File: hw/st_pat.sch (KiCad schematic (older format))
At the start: 18 parts, among them J1 Feather Left, J2 Feather Right, J3 SHARP Display, J4 BATTERY, J5 Compass Left, J6 Compass Right, SW1 SW_PWR, SW2 BTN_RST, SW3 BTN, SW4 BTN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

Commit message: Found symbol and footprint for adafruit feather
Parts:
- removed J1: Feather Left, symbol Connector:Conn_01x16_Female
- removed J2: Feather Right, symbol Connector:Conn_01x12_Female
- removed SW1: SW_PWR, symbol Switch:SW_SPST
- added SW1: SW_PWR, st_pats:SW_Rocker_A22K1H-EA, symbol Switch:SW_Push_DPDT
- added U2: FEATHER_M0_BASIC_PROTO, st_pats:MODULE_FEATHER_M0_BASIC_PROTO, symbol FEATHER_M0_BASIC_PROTO:FEATHER_M0_BASIC_PROTO
- C1, C2: footprint (none) -> Capacitor_SMD:C_0805_2012Metric_Pad1.18x1.45mm_HandSolder
- D1, D2: footprint (none) -> LED_SMD:LED_1206_3216Metric_Pad1.42x1.75mm_HandSolder
- J3: footprint (none) -> Connector_PinHeader_2.54mm:PinHeader_1x09_P2.54mm_Vertical
- J4: footprint (none) -> Connector:JWT_A3963_1x02_P3.96mm_Vertical
- J5: value Compass Left -> Compass Right; footprint (none) -> Connector_PinHeader_2.54mm:PinHeader_1x04_P2.54mm_Vertical
- J6: value Compass Right -> Compass Left; footprint (none) -> Connector_PinHeader_2.54mm:PinHeader_1x06_P2.54mm_Vertical
- R1, R2: footprint (none) -> Resistor_SMD:R_0805_2012Metric_Pad1.20x1.40mm_HandSolder
- SW2, SW3, SW4, SW5: footprint (none) -> st_pats:SW_Mini_Soft
- U1: footprint (none) -> st_pats:FGPMMOPA6H
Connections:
- net labels removed: 3v3, A0, AREF, D13, D9, EN, SCI, SDA, VBAT, VBUS
- wire segments 36 -> 35
- no-connect marks 16 -> 20
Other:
- note added: "FEATHER M0 ADALOGGER"
- note removed: "FEATHER M0 ADALOGGER PINS"
- moved on the sheet: D2, J4, J5, J6, R2

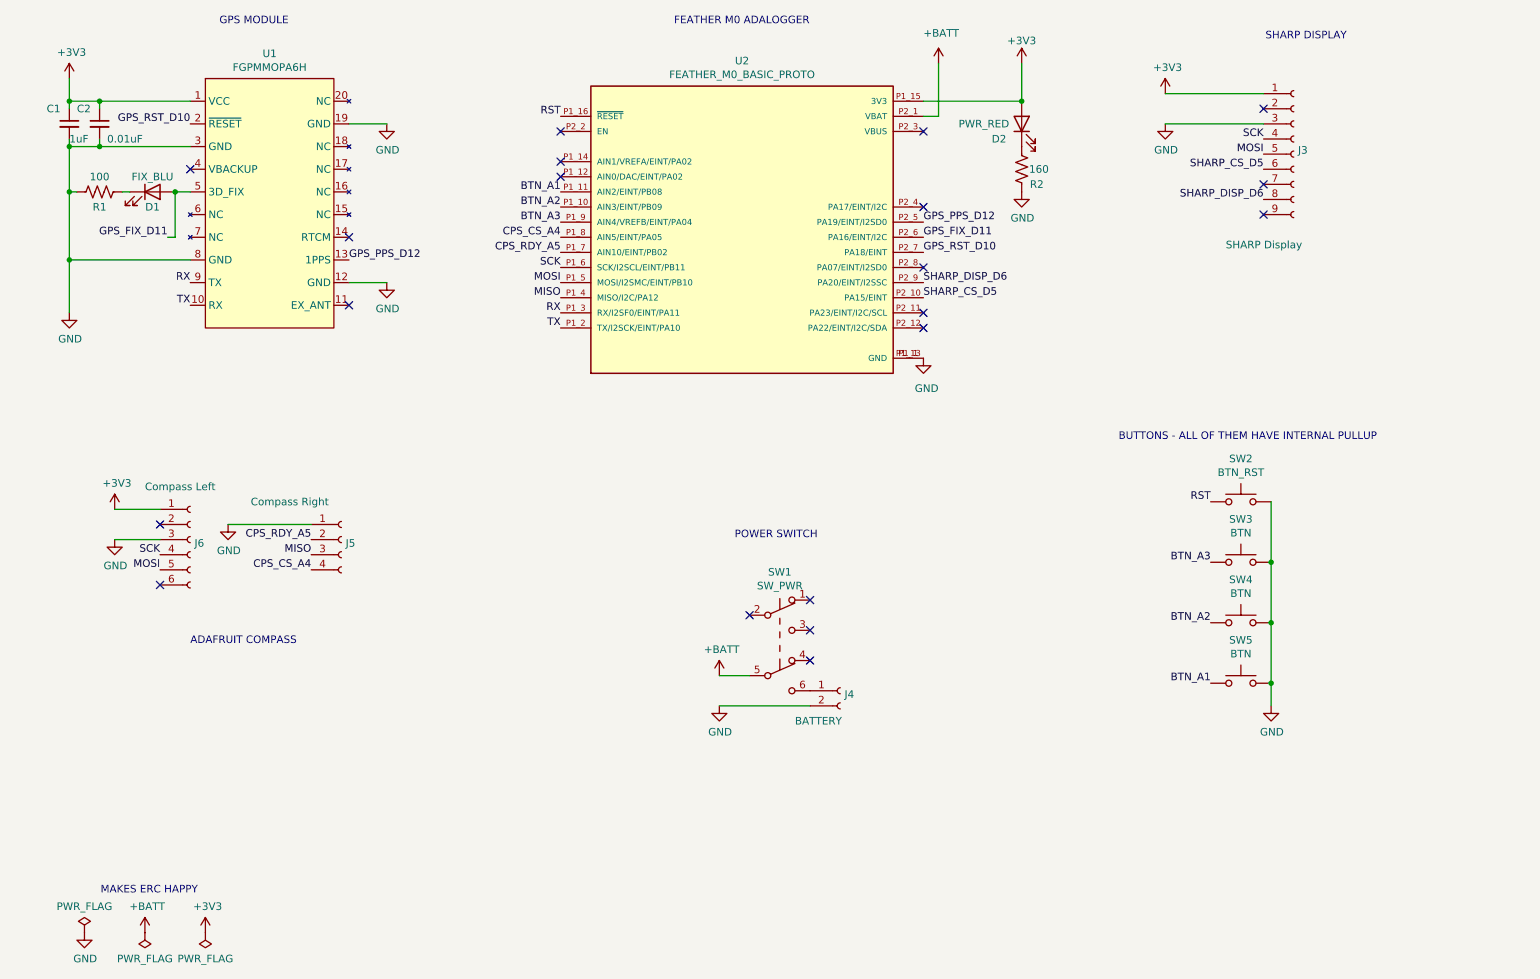
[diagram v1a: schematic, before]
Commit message: Add one more led to schematic and create pcb
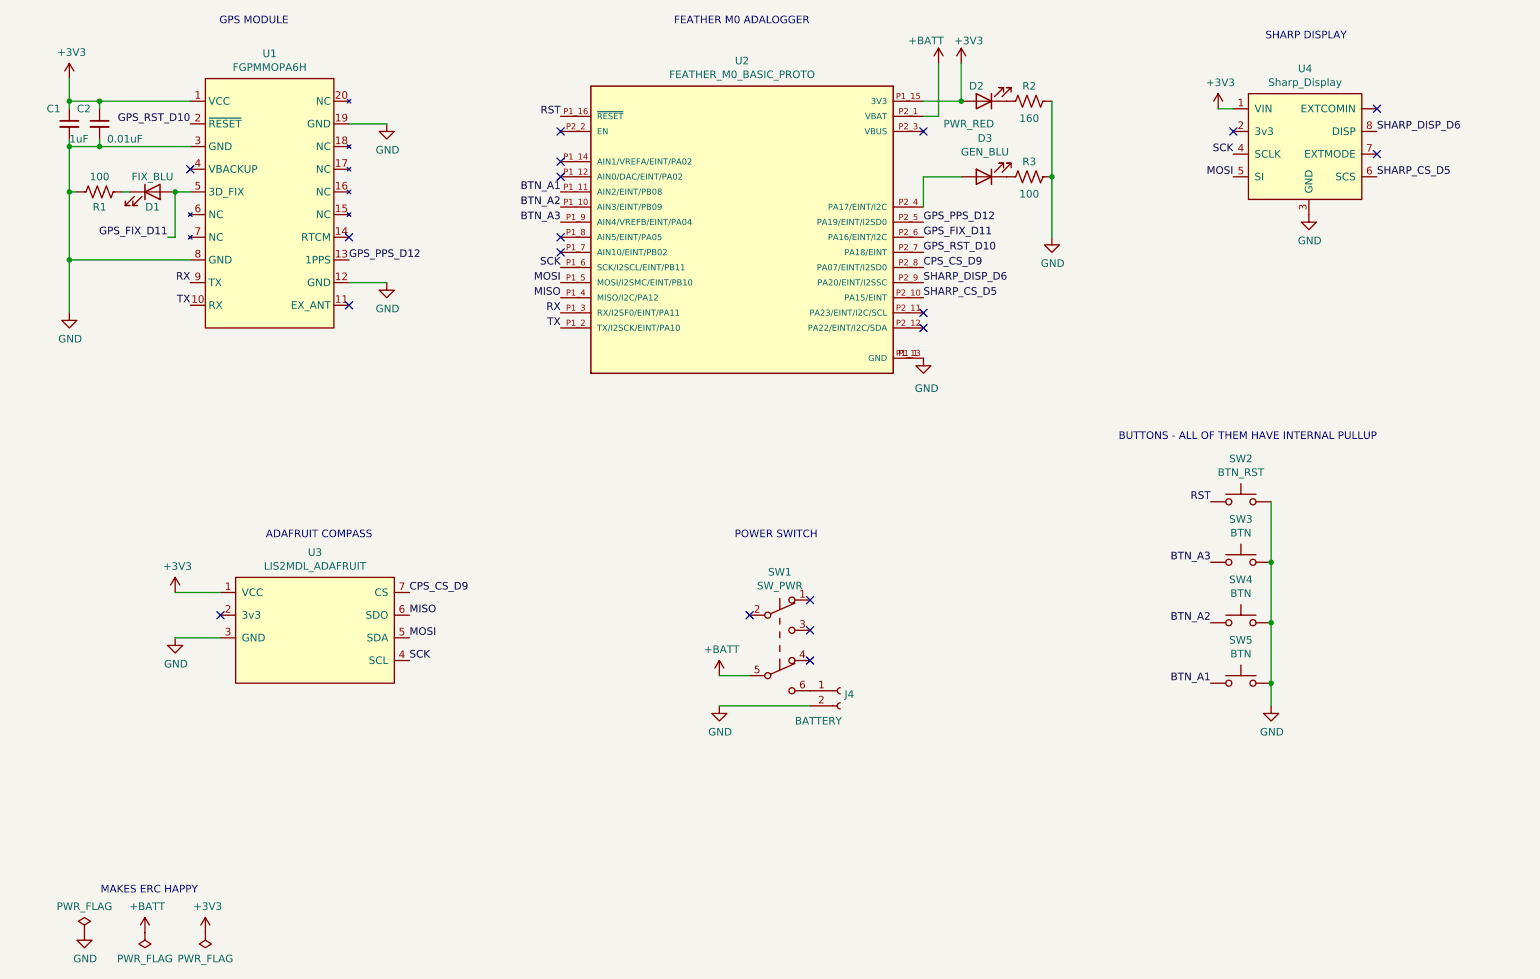
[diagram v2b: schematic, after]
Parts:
- removed J3: SHARP Display, Connector_PinHeader_2.54mm:PinHeader_1x09_P2.54mm_Vertical, symbol Connector:Conn_01x09_Female
- removed J5: Compass Right, Connector_PinHeader_2.54mm:PinHeader_1x04_P2.54mm_Vertical, symbol Connector:Conn_01x04_Female
- removed J6: Compass Left, Connector_PinHeader_2.54mm:PinHeader_1x06_P2.54mm_Vertical, symbol Connector:Conn_01x06_Female
- added D3: GEN_BLU, LED_SMD:LED_1206_3216Metric_Pad1.42x1.75mm_HandSolder, symbol Device:LED
- added R3: 100, Resistor_SMD:R_0805_2012Metric_Pad1.20x1.40mm_HandSolder, symbol Device:R_US
- added U3: LIS2MDL_ADAFRUIT, st_pat:LIS3MDL_ADAFRUIT, symbol st_pat:LIS2MDL_ADAFRUIT
- added U4: Sharp_Display, st_pat:Sharp_Display, symbol st_pat:Sharp_Display
- J4: footprint Connector:JWT_A3963_1x02_P3.96mm_Vertical -> Connector_JST:JST_PH_S2B-PH-K_1x02_P2.00mm_Horizontal
- SW1: footprint st_pats:SW_Rocker_A22K1H-EA -> st_pat:SW_Rocker_A22K1H-EA
- SW2, SW3, SW4, SW5: footprint st_pats:SW_Mini_Soft -> st_pat:SW_Mini_Soft
- U1: footprint st_pats:FGPMMOPA6H -> st_pat:FGPMMOPA6H
- U2: footprint st_pats:MODULE_FEATHER_M0_BASIC_PROTO -> FEATHER_M0_BASIC_PROTO:FEATHER_M0_BASIC_PROTO
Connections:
- net +3V3: now also U3.1 (VCC), U4.1 (VIN)
- net GND: now also R2.2, R3.2, U3.3 (GND), U4.3 (GND); no longer R2.1
- net MISO: now also U3.6 (SDO)
- net MOSI: now also U3.5 (SDA), U4.5 (SI)
- net SCK: now also U3.4 (SCL), U4.4 (SCLK)
- net SHARP_CS_D5: now also U4.6 (SCS)
- net SHARP_DISP_D6: now also U4.8 (DISP)
- net at D2.1 (K): now also R2.1; no longer R2.2
- net at U2.P2_4 (PA17/EINT/I2C): now also D3.2 (A)
- net CPS_CS_D9: now reaches U2.P2_8 (PA07/EINT/I2SD0)
- net CPS_CS_D9: now also U3.7 (CS)
- net CPS_CS_A4: no longer names the net of U2.P1_8 (AIN5/EINT/PA05)
- net CPS_RDY_A5: no longer names the net of U2.P1_7 (AIN10/EINT/PB02)
- new net: D3.1 (K), R3.1
- no-connect marks 20 -> 19
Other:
- moved on the sheet: D2, R2

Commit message: Add missing telemetry breakout board
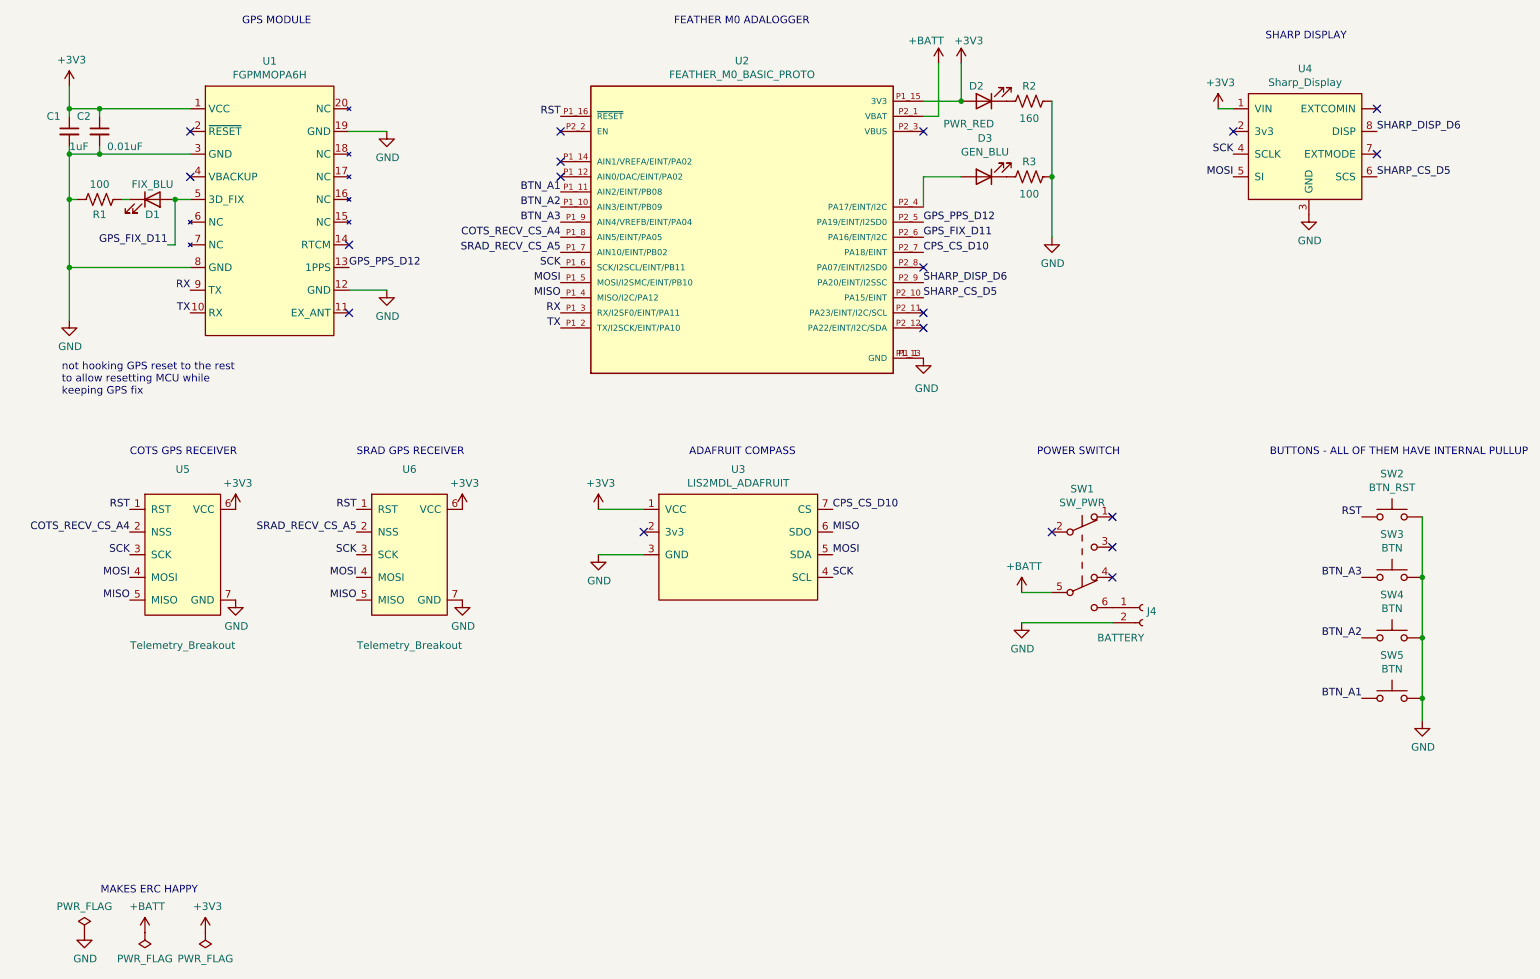
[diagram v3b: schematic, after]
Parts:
- added U5, U6: Telemetry_Breakout, st_pat:Telemetry_Breakout, symbol st_pat:Telemetry_Breakout
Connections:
- net +3V3: now also U5.6 (VCC), U6.6 (VCC)
- net GND: now also U5.7 (GND), U6.7 (GND)
- net MISO: now also U5.5 (MISO), U6.5 (MISO)
- net MOSI: now also U5.4 (MOSI), U6.4 (MOSI)
- net RST: now also U5.1 (RST), U6.1 (RST)
- net SCK: now also U5.3 (SCK), U6.3 (SCK)
- net SRAD_RECV_CS_A5: now reaches U2.P1_7 (AIN10/EINT/PB02)
- net SRAD_RECV_CS_A5: now also U6.2 (NSS)
- net COTS_RECV_CS_A4: now reaches U2.P1_8 (AIN5/EINT/PA05)
- net COTS_RECV_CS_A4: now also U5.2 (NSS)
- net CPS_CS_D9: no longer names the net of U2.P2_8 (PA07/EINT/I2SD0)
- net CPS_CS_D9: no longer U3.7 (CS)
- net GPS_RST_D10: no longer names the net of U1.2 (~RESET)
- net GPS_RST_D10: no longer U2.P2_7 (PA18/EINT)
- new net CPS_CS_D10: U2.P2_7 (PA18/EINT), U3.7 (CS)
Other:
- note added: "COTS GPS RECEIVER"
- note added: "SRAD GPS RECEIVER"
- note added: "not hooking GPS reset to the rest\nto allow resetting MCU while\nkeeping GPS fix"
- moved on the sheet: C1, C2, D1, J4, R1, SW1, SW2, SW3, SW4, SW5, U1, U3

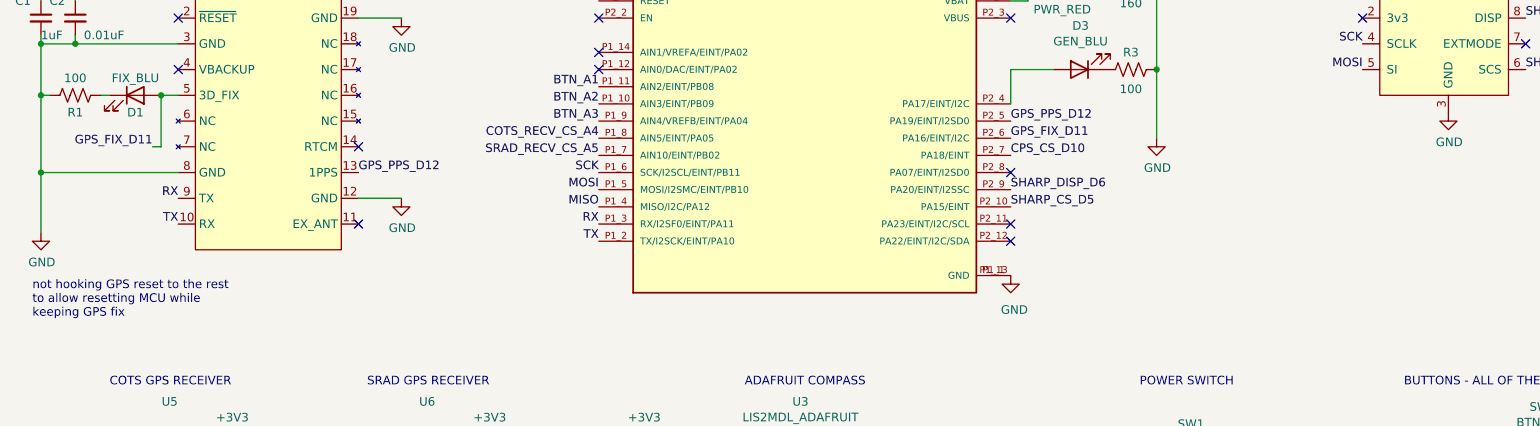
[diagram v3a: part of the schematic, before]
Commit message: Redo layout and fix some small schematic issues
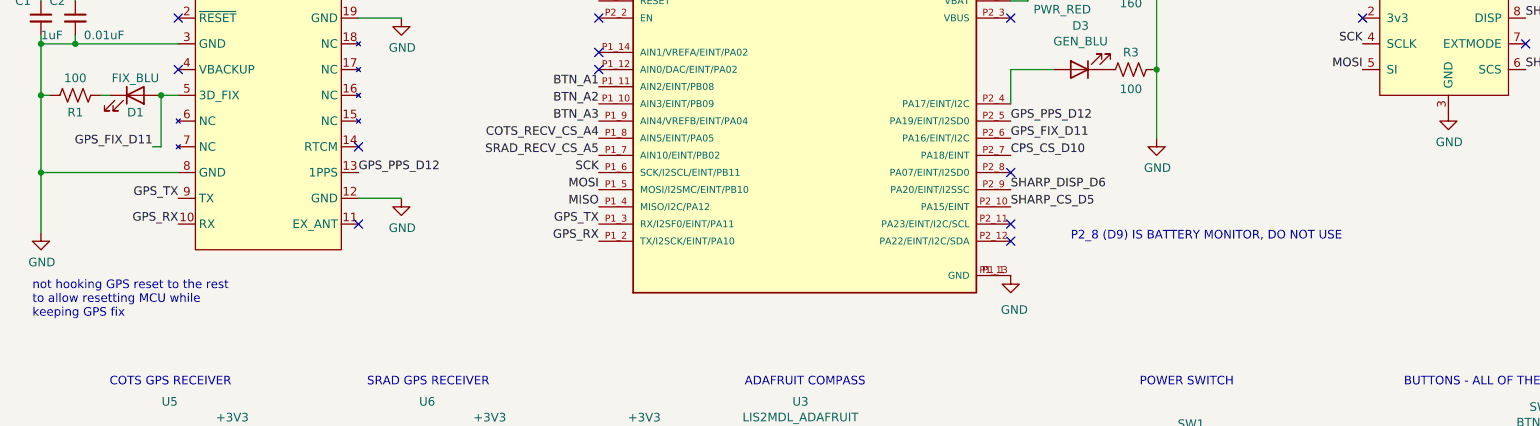
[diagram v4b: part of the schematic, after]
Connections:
- net RX renamed GPS_TX
- net TX renamed GPS_RX
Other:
- note added: "P2_8 (D9) IS BATTERY MONITOR, DO NOT USE"
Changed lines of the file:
@@
 GPS_PPS_D12
 Text Label 1750 3250 2    50   ~ 0
-TX
+GPS_RX
 Text Label 1600 2800 2    50   ~ 0
 GPS_FIX_D11
 Text Label 1750 3100 2    50   ~ 0
-RX
+GPS_TX
 Connection ~ 1150 1900
 Connection ~ 1150 2200
@@
 	6700 1950 6600 1950
 Text Label 4200 3250 2    50   ~ 0
-RX
+GPS_TX
 Text Label 4200 3350 2    50   ~ 0
-TX
+GPS_RX
 Text Label 4200 3150 2    50   ~ 0
 MISO
@@
 Text Notes 900  3800 0    50   ~ 0
 not hooking GPS reset to the rest\nto allow resetting MCU while\nkeeping GPS fix
+Text Notes 6950 3350 0    50   ~ 0
+P2_8 (D9) IS BATTERY MONITOR, DO NOT USE
 $EndSCHEMATC
